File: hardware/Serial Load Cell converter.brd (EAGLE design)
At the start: 54.6 x 40.6 mm, 51 parts, among them J1 AVR_PRG, J3 RJ11, U1 HX711, U2 ATMEGA328, U3 TMP102, U4 FT232RLSSOP, U5 MIC52055-5V, X1 USBSMD, Y2 16MHz

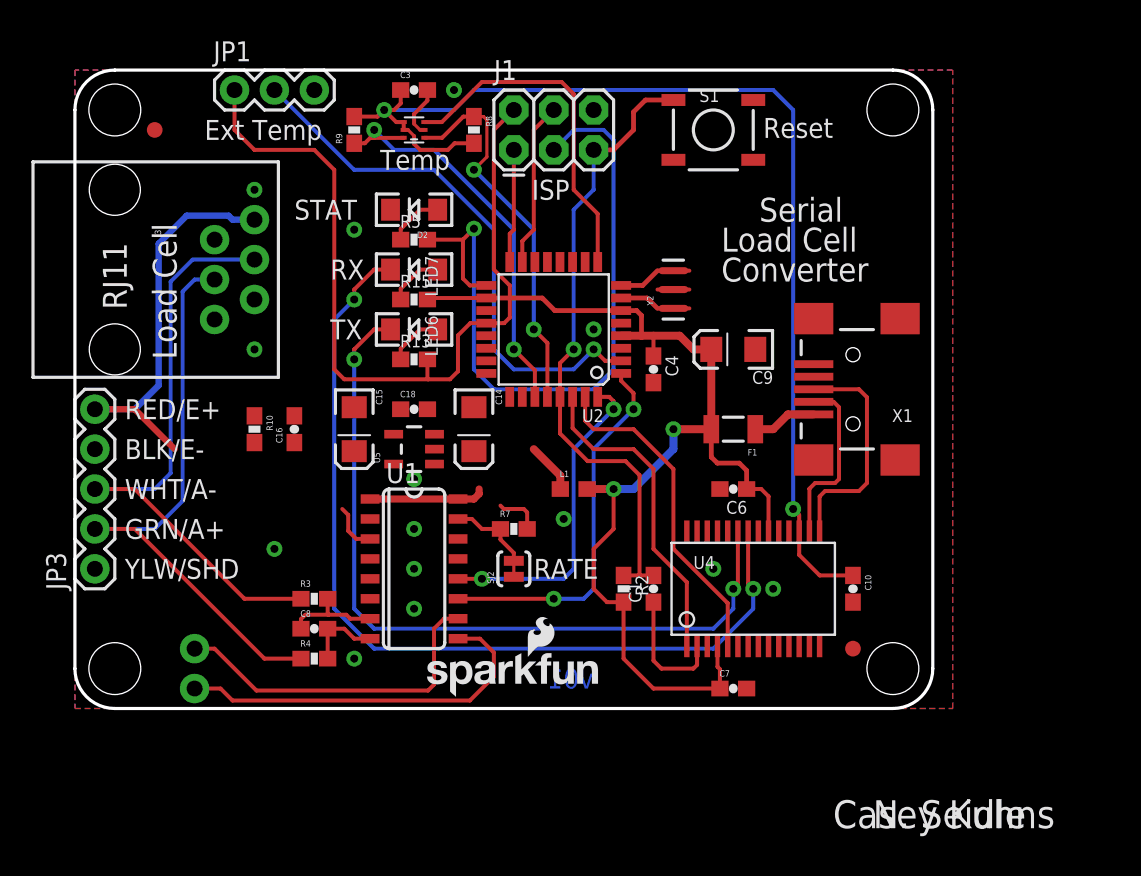
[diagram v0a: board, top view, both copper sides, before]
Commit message: Fixing file locations.
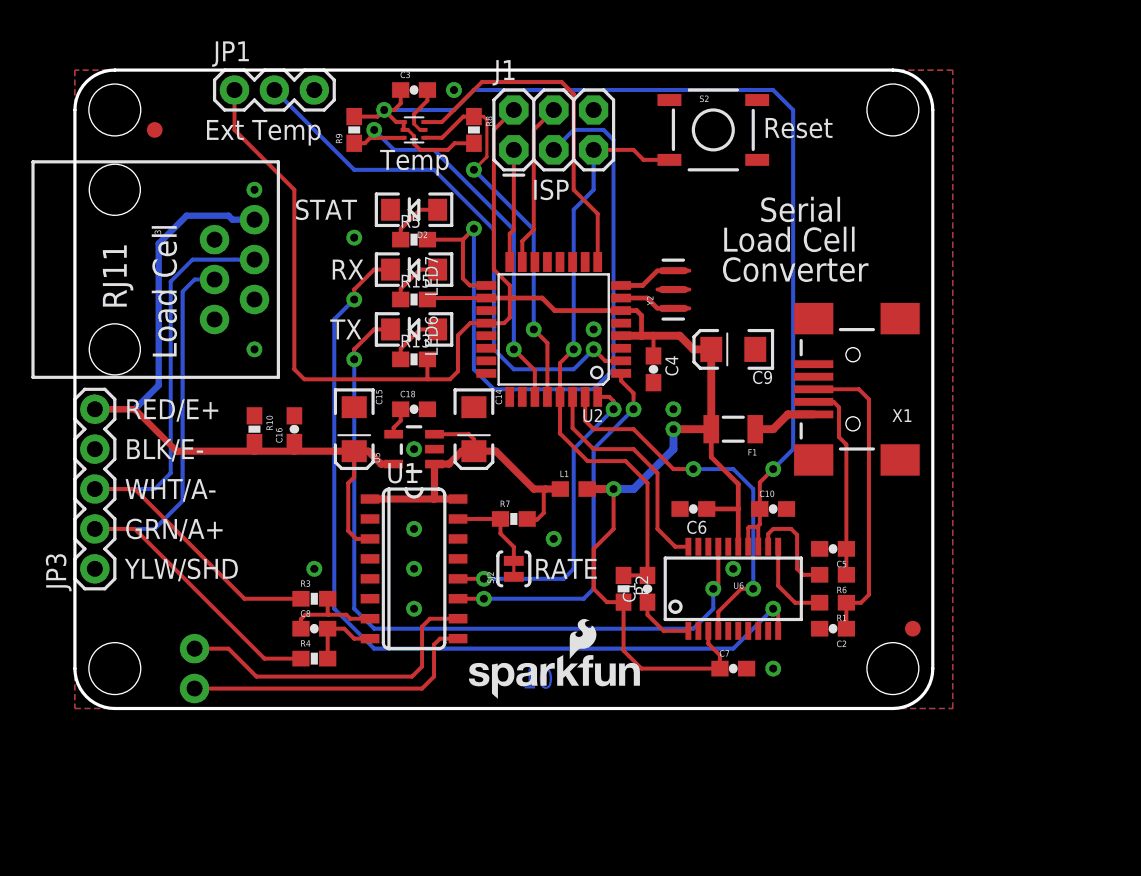
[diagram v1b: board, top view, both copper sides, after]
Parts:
- removed S1: Reset, SparkFun-Electromechanical:TACTILE_SWITCH_SMD
- removed U4: FT232RLSSOP, SparkFun-DigitalIC:SSOP28DB
- added C2, C5: 47pF, SparkFun-Capacitors:0603-CAP
- added R1, R6: 27, SparkFun-Resistors:0603
- added S2: Reset, SparkFun-Electromechanical:TACTILE-SWITCH-SMD
- added U6: FTS31X, SparkFun-DigitalIC:SSOP20_L
- D2: value RED -> BLUE
- R13, R15: value 1k -> 1K
- R2: value 10k -> 10K
- moved FRAME1 20.3 mm to (0.00, -7.62)
- moved C10 7.18 mm to (44.5, 12.7), turned to 0 degrees
- moved FID1 4.02 mm to (53.3, 5.08)
- moved C6 2.84 mm to (39.4, 12.7)
- moved LOGO1 2.67 mm to (24.6, 0.51)
- moved C7 1.27 mm to (41.9, 2.54)
- moved R7 0.63 mm to (27.9, 12.1)
- moved C1 0.38 mm to (36.4, 7.62)
- moved LOGO4 0.20 mm to (33.1, 18.7)
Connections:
- removed net USB_D+: U4.15, X1.D+
- removed net USB_D-: U4.16, X1.D-
- new net N$13: R1.2, U6.11
- new net N$4: C5.1, R6.1, X1.D-
- new net N$7: C2.1, R1.1, X1.D+
- new net N$8: R6.2, U6.12
- net 3.3V: now also U6.13, U6.14; no longer U4.17
- net 5V: now also U6.15, U6.3; no longer U4.20, U4.4
- net DTR: now also U6.1; no longer U4.2
- net GND: now also C2.2, C5.2, S2.1, U6.16, U6.6; no longer S1.3, S1.4, U4.18, U4.21, U4.25, U4.26, U4.7
- net RST: now also S2.3; no longer S1.1
- net RXD: now also U6.20; no longer U4.1
- net RXLED: now also LED6.C, U6.17; no longer LED7.C, U4.22
- net TXD: now also U6.4; no longer U4.5
- net TXLED: now also LED7.C, U6.10; no longer LED6.C, U4.23
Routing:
- net N$7: track 0.00 -> 19.5 mm
- net AVDD: track 29.9 -> 49.1 mm
- net USB_D+: track 14.6 -> 0.00 mm
- net N$4: track 0.00 -> 12.6 mm
- net USB_D-: track 11.2 -> 0.00 mm
- net RXLED: track 57.5 -> 47.3 mm
- net VCC: track 13.6 -> 23.4 mm
- net N$8: track 0.00 -> 6.70 mm
- net RXD: track 20.4 -> 14.6 mm
- net TXLED: track 49.6 -> 55.3 mm
- net N$13: track 0.00 -> 5.58 mm
- net B-: track 24.2 -> 19.3 mm
- net DTR: track 7.99 -> 3.83 mm
- net TXD: track 21.1 -> 24.4 mm, vias 0 -> 2
- net RST: track 40.5 -> 38.3 mm
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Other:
- board text removed: "Casey Kuhns"
- board text removed: "N. Seidle"
- board text removed: "v01"

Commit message: Added external serial connection.
Can be used to emergency reset the serial interface back to 9600bps.
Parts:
- added JP4: (no value), SparkFun-Connectors:1X04
- added R11, R12: 1K, SparkFun-Resistors:0603-RES
- moved FID1 5.39 mm to (49.5, 1.27)
- moved C1 2.69 mm to (35.6, 5.08), turned to 180 degrees
- moved FID2 2.54 mm to (5.08, 39.4)
- moved F1 1.27 mm to (41.9, 19.1)
- moved X1 1.27 mm to (49.5, 21.6)
- moved R2 1.09 mm to (35.6, 6.73), turned to 0 degrees
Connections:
- new net N$14: R12.2, U6.4
- new net N$16: R11.2, U6.20
- net 5V: now also JP4.2
- net GND: now also JP4.1
- net RXD: now also JP4.3, R11.1; no longer U6.20
- net TXD: now also JP4.4, R12.1; no longer U6.4
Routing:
- net RXD: track 14.6 -> 30.5 mm, vias 0 -> 1
- net 5V: track 121.6 -> 132.4 mm, vias 2 -> 3
- net TXD: track 24.4 -> 33.2 mm
- net N$14: track 0.00 -> 7.26 mm
- net N$16: track 0.00 -> 2.70 mm
- net RST: track 38.3 -> 41.0 mm, vias 1 -> 3
- net N$4: track 12.6 -> 13.9 mm
- net DTR: track 3.83 -> 2.70 mm
- net N$7: track 19.5 -> 20.6 mm

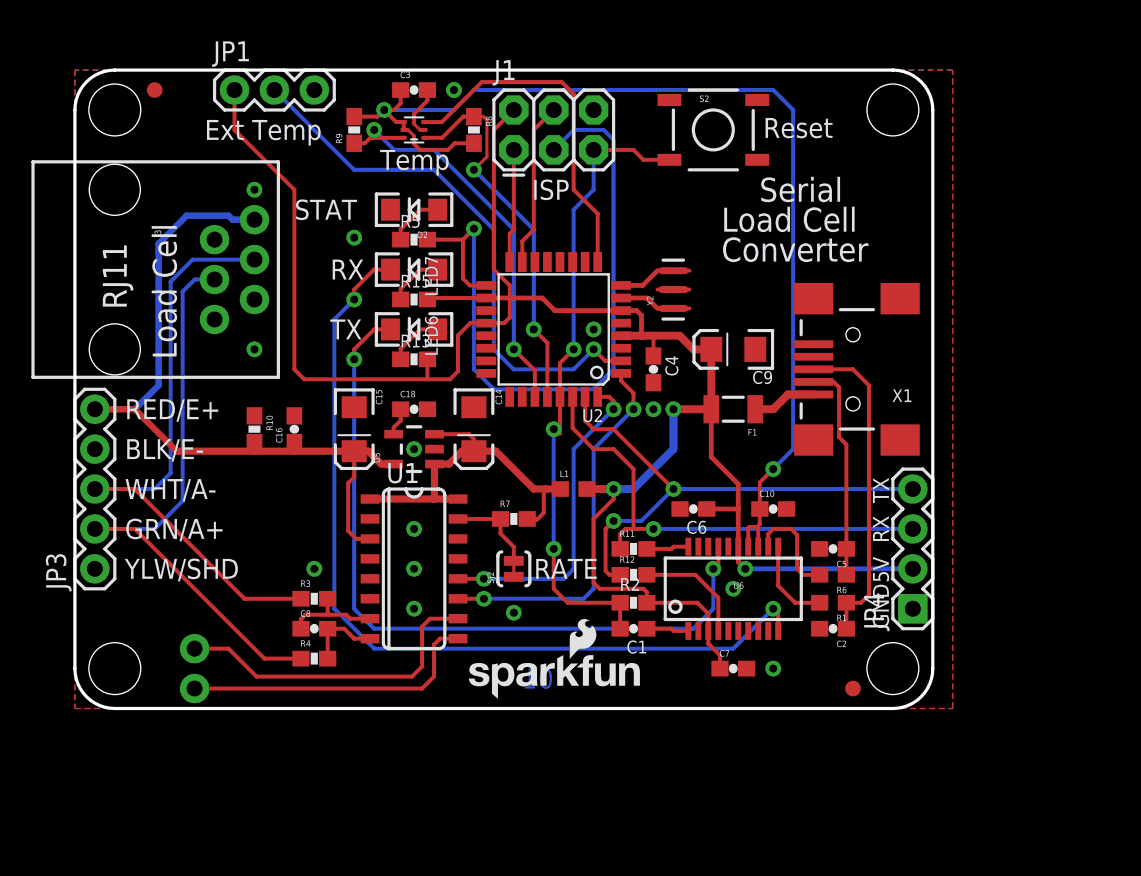
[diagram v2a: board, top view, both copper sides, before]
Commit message: First round of fixes from PLewis review
Fixed J1/J3 labels on schematic. Fixed LED colors to match standards.
Added test point for VCC. Improved layout around TMP102. Added measures.
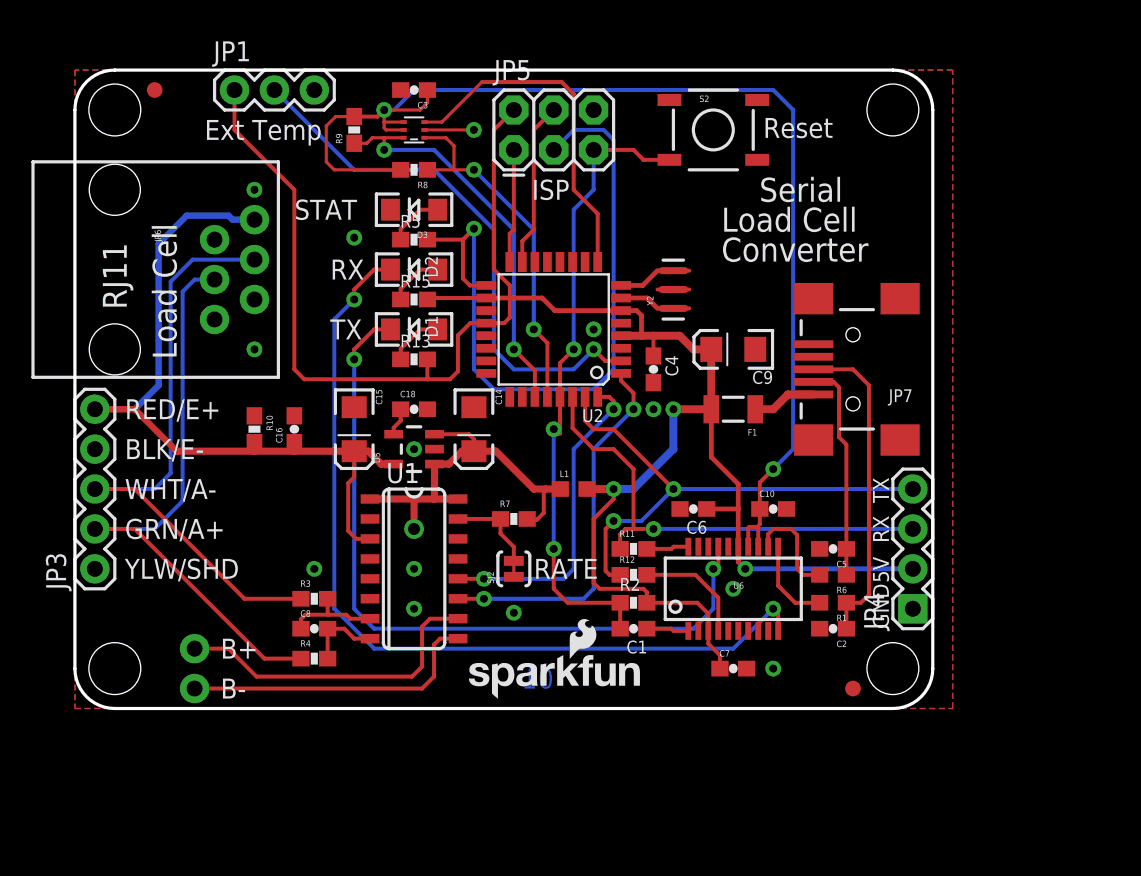
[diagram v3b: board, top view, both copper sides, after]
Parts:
- removed LED7: GREEN, SparkFun-LED:LED-1206
- added D3: BLUE, SparkFun-LED:LED-1206
- D1: value RED -> YELLOW
- D2: value BLUE -> GREEN
- moved R8 4.58 mm to (21.6, 34.3), turned to 180 degrees
- moved D2 3.81 mm to (21.6, 27.9)
- turned C3 to 180 degrees
- renumbered J1 to JP5, J3 to JP6, LED6 to D1, X1 to JP7
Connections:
- net GND: now also D3.C; no longer D2.C
- net N$2: now also D3.A; no longer D2.A
- net N$6: now also D2.A; no longer LED7.A
- net TXLED: now also D2.C; no longer LED7.C
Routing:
- net 3.3V: track 69.3 -> 76.4 mm
- net VCC: track 23.4 -> 25.3 mm, vias 0 -> 1
- net SCL: track 24.5 -> 23.0 mm
- net SDA: track 26.5 -> 25.6 mm
- net GND: track 3.33 -> 3.15 mm, vias 14 -> 13
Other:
- board text removed: "Temp"

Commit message: Fixing issue #1
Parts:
- U4: value ATMEGA328 -> ATMEGA328P_TQFP
- U6: value FTS31X -> FT231X
- Y2: value 16MHz -> 16MHZ
- moved R12 3.43 mm to (35.6, 5.08)
- moved R2 1.78 mm to (35.6, 8.51)
- moved C1 1.78 mm to (35.6, 6.86)
- renumbered U2 to U4
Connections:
- net 3.3V: now also U6.3
- net 5V: no longer U6.3
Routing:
- net TXD: track 33.2 -> 41.6 mm
- net 3.3V: track 76.4 -> 80.3 mm
- net GND: track 3.15 -> 6.46 mm, vias 13 -> 16
- net RST: track 41.0 -> 38.6 mm
- net N$16: track 2.70 -> 4.38 mm
- net DTR: track 2.70 -> 4.23 mm
- net 5V: track 132.4 -> 133.4 mm, vias 3 -> 4
- net N$14: track 7.26 -> 6.70 mm
